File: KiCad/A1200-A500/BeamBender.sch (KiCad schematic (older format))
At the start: 36 parts, among them J1 4-1734742-0, J2 HDMI_A_1.4, J3 STX-3501-3N, J4 Phoenix_Contact, U1 LM1117-3.3, U3 ADV7513BSWZ, X1 Abracon ASE-27.000MHZ-L-R-T

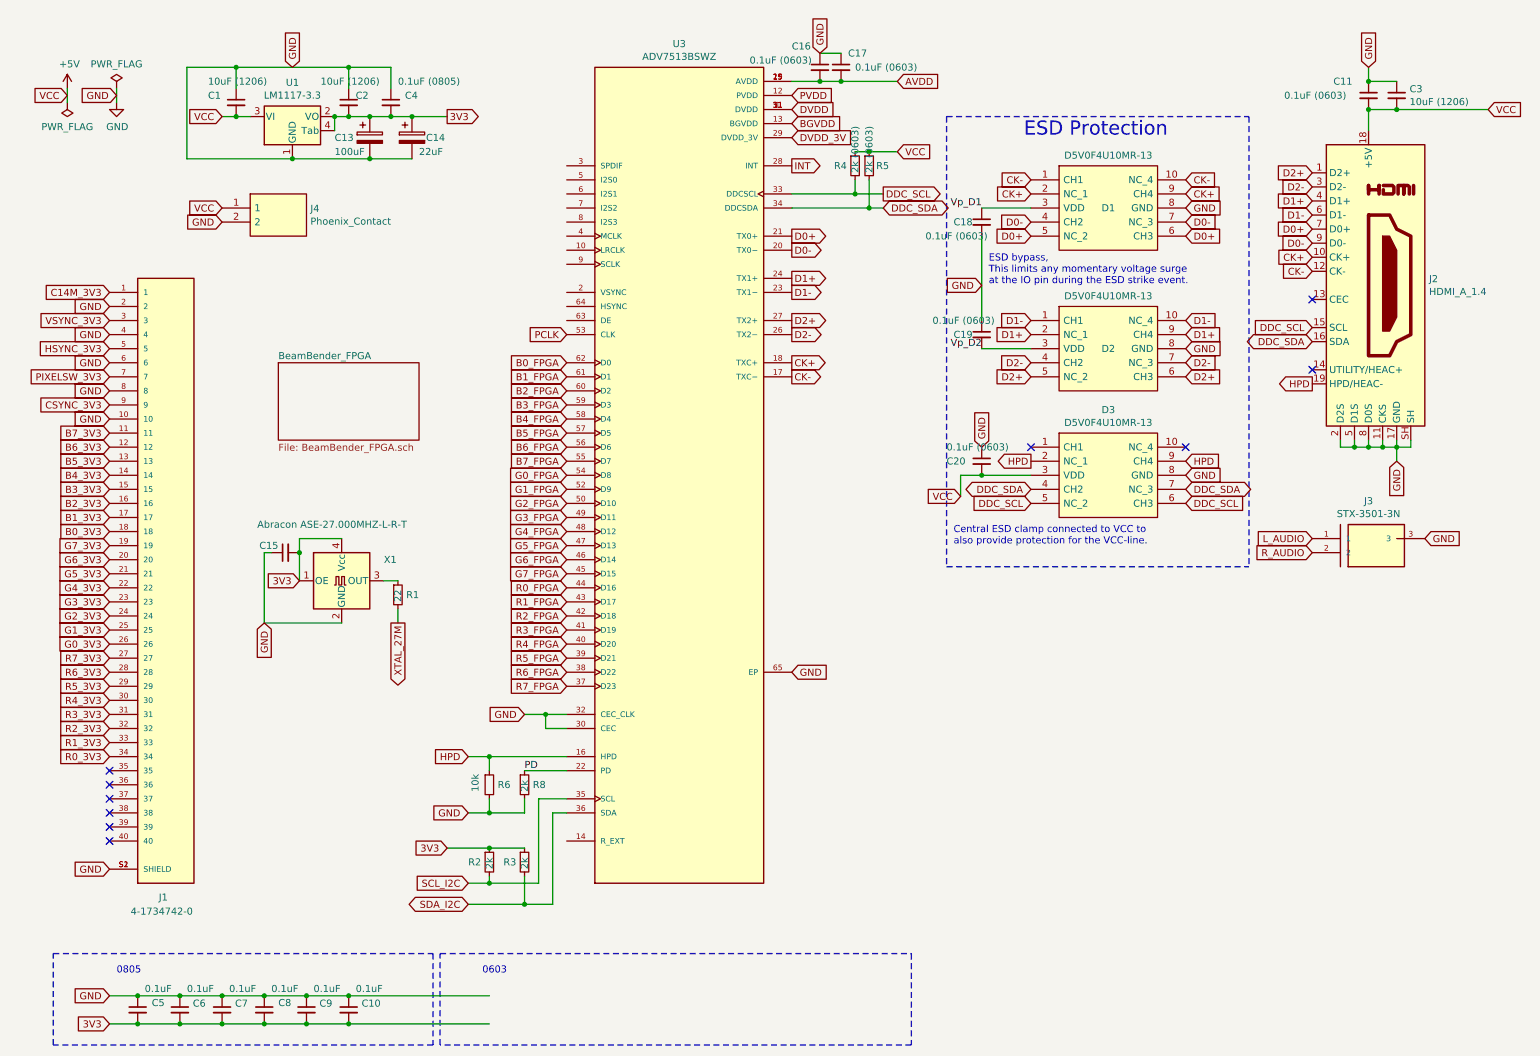
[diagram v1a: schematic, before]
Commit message: more place and route of pull-ups for SDL,SDA,DDC_SDL and DDC_SDA around ADV7513 chip
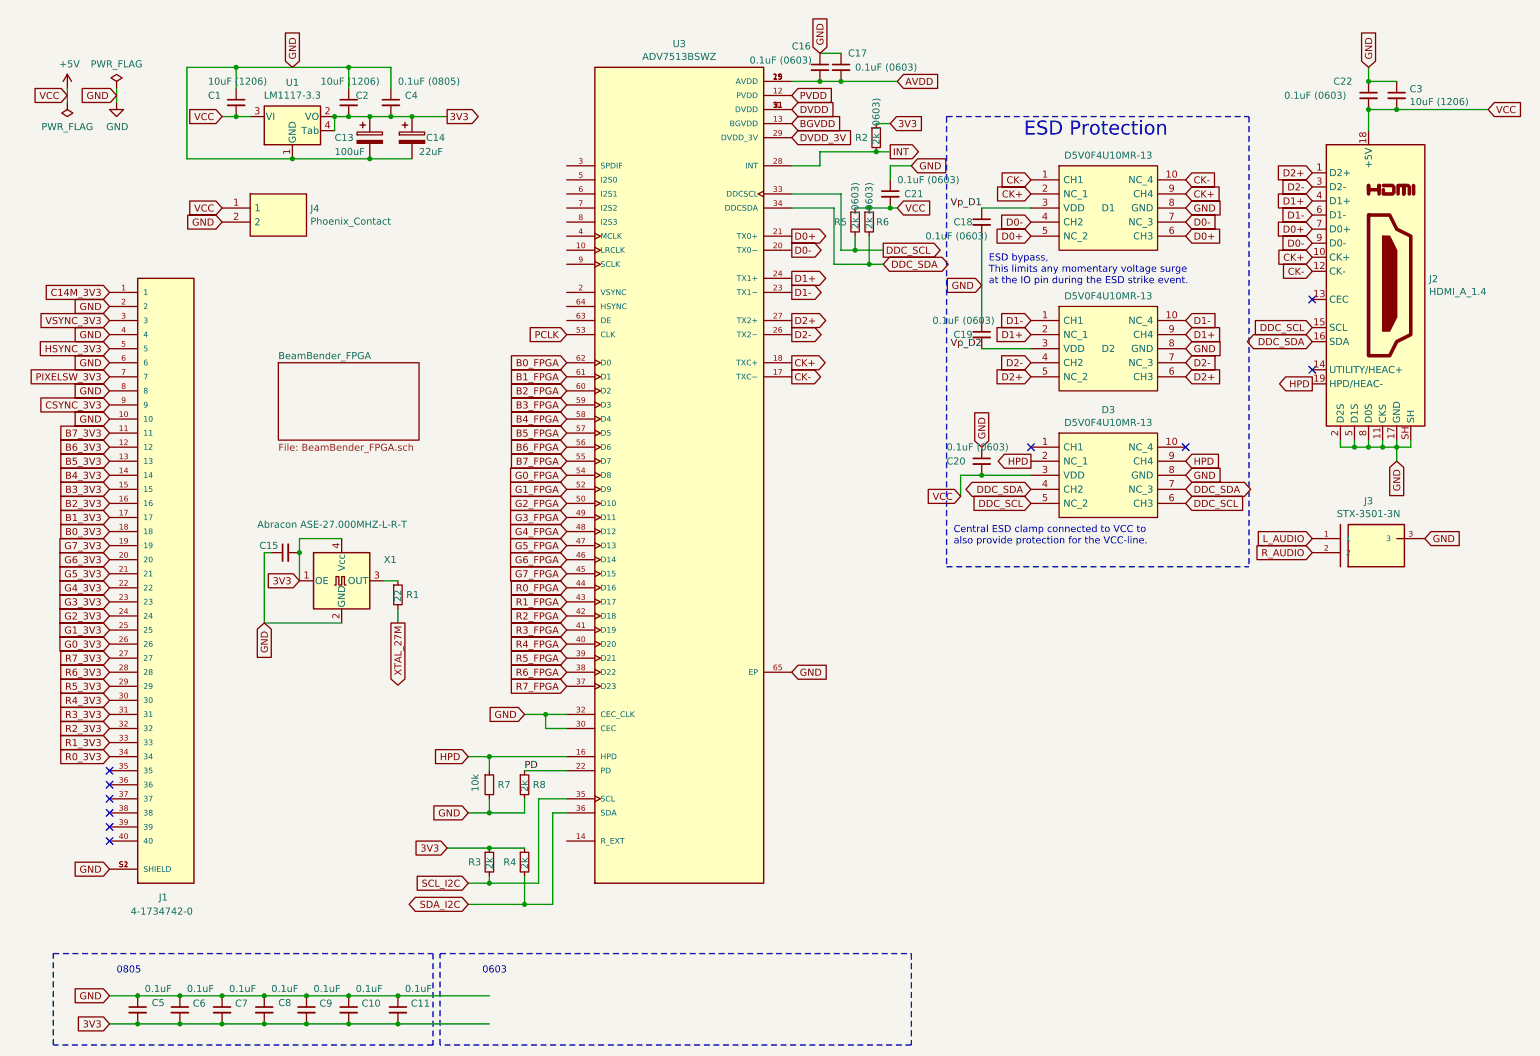
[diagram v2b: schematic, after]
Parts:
- added C11: 0.1uF, Capacitor_SMD:C_0805_2012Metric_Pad1.18x1.45mm_HandSolder, symbol Device:C_Small
- added C21: 0.1uF (0603), Capacitor_SMD:C_0603_1608Metric_Pad1.08x0.95mm_HandSolder, symbol Device:C_Small
- added R2: 2k (0603), Resistor_SMD:R_0603_1608Metric_Pad0.98x0.95mm_HandSolder, symbol Device:R_Small
- renumbered C11 to C22, R2 to R3, R3 to R4, R4 to R5, R5 to R6, R6 to R7
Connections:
- net +5V: now also C21.2
- net 3V3: now also C11.2, R2.1
- net GND: now also C11.1, C21.1
- net INT: now also R2.2
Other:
- moved on the sheet: R5, R6
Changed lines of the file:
@@
 Wire Wire Line
 	10300 3500 10300 3600
-Text GLabel 6650 1700 2    50   Output ~ 0
+Text GLabel 6650 2100 2    50   Output ~ 0
 DDC_SCL
-Text GLabel 6650 1800 2    50   BiDi ~ 0
+Text GLabel 6650 2200 2    50   BiDi ~ 0
 DDC_SDA
 Text GLabel 9700 2750 0    50   BiDi ~ 0
@@
 GND
 $Comp
-L Device:R_Small R4
+L Device:R_Small R5
 U 1 1 6532D8B1
-P 6450 1500
-F 0 "R4" H 6300 1500 50  0000 L CNN
-F 1 "2k  (0603)" V 6450 1450 50  0000 L CNN
-F 2 "Resistor_SMD:R_0603_1608Metric_Pad0.98x0.95mm_HandSolder" H 6450 1500 50  0001 C CNN
-F 3 "~" H 6450 1500 50  0001 C CNN
-	1    6450 1500
-	1    0    0    -1
-$EndComp
-Text GLabel 6750 1400 2    50   Input ~ 0
+P 6450 1900
+F 0 "R5" H 6300 1900 50  0000 L CNN
+F 1 "2k  (0603)" V 6450 1850 50  0000 L CNN
+F 2 "Resistor_SMD:R_0603_1608Metric_Pad0.98x0.95mm_HandSolder" H 6450 1900 50  0001 C CNN
+F 3 "~" H 6450 1900 50  0001 C CNN
+	1    6450 1900
+	1    0    0    -1
+$EndComp
+Text GLabel 6750 1800 2    50   Input ~ 0
 VCC
 Wire Wire Line
-	6450 1600 6450 1700
-Connection ~ 6450 1700
-Wire Wire Line
-	6450 1700 6650 1700
-Wire Wire Line
-	6550 1600 6550 1800
-Connection ~ 6550 1800
-Wire Wire Line
-	6550 1800 6650 1800
+	6450 2000 6450 2100
+Wire Wire Line
+	6450 2100 6650 2100
+Wire Wire Line
+	6550 2000 6550 2200
+Wire Wire Line
+	6550 2200 6650 2200
 Text GLabel 9700 2650 0    50   Input ~ 0
 DDC_SCL
-Wire Wire Line
-	6000 1700 6450 1700
-Wire Wire Line
-	6000 1800 6550 1800
 Text GLabel 4400 2900 0    50   Input ~ 0
 B0_FPGA
@@
 Vp_D1
 $Comp
-L Device:C_Small C11
+L Device:C_Small C22
 U 1 1 654A833A
 P 10100 1000
-F 0 "C11" H 9850 1100 50  0000 L CNN
+F 0 "C22" H 9850 1100 50  0000 L CNN
 F 1 "0.1uF (0603)" H 9500 1000 50  0000 L CNN
 F 2 "Capacitor_SMD:C_0603_1608Metric_Pad1.08x0.95mm_HandSolder" H 10100 1000 50  0001 C CNN
@@
 Connection ~ 3300 1150
 $Comp
-L Device:R_Small R5
+L Device:R_Small R6
 U 1 1 6532BC2D
-P 6550 1500
-F 0 "R5" H 6600 1500 50  0000 L CNN
-F 1 "2k  (0603)" V 6550 1450 50  0000 L CNN
-F 2 "Resistor_SMD:R_0603_1608Metric_Pad0.98x0.95mm_HandSolder" H 6550 1500 50  0001 C CNN
-F 3 "~" H 6550 1500 50  0001 C CNN
-	1    6550 1500
+P 6550 1900
+F 0 "R6" H 6600 1900 50  0000 L CNN
+F 1 "2k  (0603)" V 6550 1850 50  0000 L CNN
+F 2 "Resistor_SMD:R_0603_1608Metric_Pad0.98x0.95mm_HandSolder" H 6550 1900 50  0001 C CNN
+F 3 "~" H 6550 1900 50  0001 C CNN
+	1    6550 1900
 	1    0    0    -1
 $EndComp
@@
 	10300 1100 10950 1100
 Wire Wire Line
-	6450 1400 6550 1400
-Connection ~ 6550 1400
-Wire Wire Line
-	6550 1400 6750 1400
+	6450 1800 6550 1800
+Connection ~ 6550 1800
+Wire Wire Line
+	6550 1800 6700 1800
 Text Notes 1200 7250 0    50   ~ 0
 0805
@@
 GND
 $Comp
-L Device:R_Small R6
+L Device:R_Small R7
 U 1 1 652DC9C5
 P 3850 5900
-F 0 "R6" H 3909 5900 50  0000 L CNN
+F 0 "R7" H 3909 5900 50  0000 L CNN
 F 1 "10k" V 3750 5850 50  0000 L CNN
 F 2 "Resistor_SMD:R_0603_1608Metric_Pad0.98x0.95mm_HandSolder" H 3850 5900 50  0001 C CNN
@@
 	4300 6100 4400 6100
 $Comp
-L Device:R_Small R2
+L Device:R_Small R3
 U 1 1 655C6F45
 P 3850 6450
-F 0 "R2" H 3700 6450 50  0000 L CNN
+F 0 "R3" H 3700 6450 50  0000 L CNN
 F 1 "2k" V 3850 6400 50  0000 L CNN
 F 2 "Resistor_SMD:R_0603_1608Metric_Pad0.98x0.95mm_HandSolder" H 3850 6450 50  0001 C CNN
@@
 	3850 6600 4200 6600
 $Comp
-L Device:R_Small R3
+L Device:R_Small R4
 U 1 1 655D3232
 P 4100 6450
-F 0 "R3" H 3950 6450 50  0000 L CNN
+F 0 "R4" H 3950 6450 50  0000 L CNN
 F 1 "2k" V 4100 6400 50  0000 L CNN
 F 2 "Resistor_SMD:R_0603_1608Metric_Pad0.98x0.95mm_HandSolder" H 4100 6450 50  0001 C CNN
@@
 Wire Wire Line
 	2550 7600 2850 7600
-Text GLabel 6000 1500 2    50   Output ~ 0
+Text GLabel 6700 1400 2    50   Output ~ 0
 INT
 Text GLabel 6000 1000 2    50   Input ~ 0
@@
 Connection ~ 2850 7400
 Wire Wire Line
-	2850 7400 3850 7400
+	2850 7400 3200 7400
 Connection ~ 2850 7600
 Wire Wire Line
-	2850 7600 3850 7600
+	2850 7600 3200 7600
 Text GLabel 4400 2700 0    50   Input ~ 0
 PCLK
+$Comp
+L Device:R_Small R2
+U 1 1 656847D2
+P 6600 1300
+F 0 "R2" H 6450 1300 50  0000 L CNN
+F 1 "2k  (0603)" V 6600 1250 50  0000 L CNN
+F 2 "Resistor_SMD:R_0603_1608Metric_Pad0.98x0.95mm_HandSolder" H 6600 1300 50  0001 C CNN
+F 3 "~" H 6600 1300 50  0001 C CNN
+	1    6600 1300
+	1    0    0    -1
+$EndComp
+Wire Wire Line
+	6450 2100 6350 2100
+Wire Wire Line
+	6350 2100 6350 1700
+Wire Wire Line
+	6350 1700 6000 1700
+Connection ~ 6450 2100
+Wire Wire Line
+	6000 1800 6300 1800
+Wire Wire Line
+	6300 1800 6300 2200
+Wire Wire Line
+	6300 2200 6550 2200
+Connection ~ 6550 2200
+Text GLabel 6700 1200 2    50   Input ~ 0
+3V3
+Wire Wire Line
+	6600 1200 6700 1200
+$Comp
+L Device:C_Small C11
+U 1 1 656BAD96
+P 3200 7500
+F 0 "C11" H 3292 7546 50  0000 L CNN
+F 1 "0.1uF" H 3250 7650 50  0000 L CNN
+F 2 "Capacitor_SMD:C_0805_2012Metric_Pad1.18x1.45mm_HandSolder" H 3200 7500 50  0001 C CNN
+F 3 "~" H 3200 7500 50  0001 C CNN
+	1    3200 7500
+	1    0    0    -1
+$EndComp
+Connection ~ 3200 7400
+Wire Wire Line
+	3200 7400 3850 7400
+Connection ~ 3200 7600
+Wire Wire Line
+	3200 7600 3850 7600
+$Comp
+L Device:C_Small C21
+U 1 1 656E4A42
+P 6700 1700
+F 0 "C21" H 6800 1700 50  0000 L CNN
+F 1 "0.1uF (0603)" H 6750 1800 50  0000 L CNN
+F 2 "Capacitor_SMD:C_0603_1608Metric_Pad1.08x0.95mm_HandSolder" H 6700 1700 50  0001 C CNN
+F 3 "~" H 6700 1700 50  0001 C CNN
+	1    6700 1700
+	1    0    0    -1
+$EndComp
+Connection ~ 6700 1800
+Wire Wire Line
+	6700 1800 6750 1800
+Text GLabel 6850 1500 2    50   Input ~ 0
+GND
+Wire Wire Line
+	6000 1500 6200 1500
+Wire Wire Line
+	6200 1500 6200 1400
+Wire Wire Line
+	6200 1400 6600 1400
+Wire Wire Line
+	6700 1600 6700 1500
+Wire Wire Line
+	6700 1500 6850 1500
+Wire Wire Line
+	6600 1400 6700 1400
+Connection ~ 6600 1400
 $EndSCHEMATC

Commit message: more routing done
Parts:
- added C12: 10uF (1206), Capacitor_SMD:C_1206_3216Metric_Pad1.33x1.80mm_HandSolder, symbol Device:C_Small
- added C23: 0.1uF (0603), Capacitor_SMD:C_0603_1608Metric_Pad1.08x0.95mm_HandSolder, symbol Device:C_Small
- added C?: 0.1uF, Capacitor_SMD:C_0603_1608Metric_Pad1.08x0.95mm_HandSolder, symbol Device:C_Small
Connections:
- net 3V3: now also C?.2
- net DVDD: now also C12.1, C23.1
- net GND: now also C12.2, C23.2, C?.1
- net VSYNC_FPGA: now reaches U3.2 (VSYNC)
- net DE: now reaches U3.63 (DE)
- net HSYNC_FPGA: now reaches U3.64 (HSYNC)
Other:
- moved on the sheet: C11
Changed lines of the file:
@@
 	10200 3500 10300 3500
 NoConn ~ 9700 2950
-Text GLabel 6750 900  2    50   Input ~ 0
-AVDD
 Wire Wire Line
 	6000 900  6200 900
@@
 Wire Wire Line
 	6200 900  6350 900
-$Comp
-L Device:C_Small C17
-U 1 1 653F698E
-P 6350 800
-F 0 "C17" H 6400 900 50  0000 L CNN
-F 1 "0.1uF (0603)" H 6450 800 50  0000 L CNN
-F 2 "Capacitor_SMD:C_0603_1608Metric_Pad1.08x0.95mm_HandSolder" H 6350 800 50  0001 C CNN
-F 3 "~" H 6350 800 50  0001 C CNN
-	1    6350 800
-	1    0    0    -1
-$EndComp
-Connection ~ 6350 900
-Wire Wire Line
-	6350 900  6750 900
 Wire Wire Line
 	6200 700  6350 700
@@
 Text GLabel 6000 1000 2    50   Input ~ 0
 PVDD
-Text GLabel 6000 1100 2    50   Input ~ 0
-DVDD
 Text GLabel 6000 1300 2    50   Input ~ 0
 DVDD_3V
@@
 Connection ~ 2850 7400
 Wire Wire Line
-	2850 7400 3200 7400
+	2850 7400 3150 7400
 Connection ~ 2850 7600
 Wire Wire Line
-	2850 7600 3200 7600
+	2850 7600 3150 7600
 Text GLabel 4400 2700 0    50   Input ~ 0
 PCLK
@@
 L Device:C_Small C11
 U 1 1 656BAD96
-P 3200 7500
-F 0 "C11" H 3292 7546 50  0000 L CNN
-F 1 "0.1uF" H 3250 7650 50  0000 L CNN
-F 2 "Capacitor_SMD:C_0805_2012Metric_Pad1.18x1.45mm_HandSolder" H 3200 7500 50  0001 C CNN
-F 3 "~" H 3200 7500 50  0001 C CNN
-	1    3200 7500
-	1    0    0    -1
-$EndComp
-Connection ~ 3200 7400
-Wire Wire Line
-	3200 7400 3850 7400
-Connection ~ 3200 7600
-Wire Wire Line
-	3200 7600 3850 7600
+P 3150 7500
+F 0 "C11" H 3242 7546 50  0000 L CNN
+F 1 "0.1uF" H 3200 7650 50  0000 L CNN
+F 2 "Capacitor_SMD:C_0805_2012Metric_Pad1.18x1.45mm_HandSolder" H 3150 7500 50  0001 C CNN
+F 3 "~" H 3150 7500 50  0001 C CNN
+	1    3150 7500
+	1    0    0    -1
+$EndComp
 $Comp
 L Device:C_Small C21
@@
 	6600 1400 6700 1400
 Connection ~ 6600 1400
+Connection ~ 3150 7400
+Connection ~ 3150 7600
+Wire Wire Line
+	3150 7400 3850 7400
+Wire Wire Line
+	3150 7600 3850 7600
+$Comp
+L Device:C_Small C17
+U 1 1 653F698E
+P 6350 800
+F 0 "C17" H 6400 900 50  0000 L CNN
+F 1 "0.1uF (0603)" H 6450 800 50  0000 L CNN
+F 2 "Capacitor_SMD:C_0603_1608Metric_Pad1.08x0.95mm_HandSolder" H 6350 800 50  0001 C CNN
+F 3 "~" H 6350 800 50  0001 C CNN
+	1    6350 800
+	1    0    0    -1
+$EndComp
+Text GLabel 6000 1100 2    50   Input ~ 0
+DVDD
+Connection ~ 6350 900
+Wire Wire Line
+	6350 900  6750 900
+Text GLabel 6750 900  2    50   Input ~ 0
+AVDD
+$Comp
+L Device:C_Small C12
+U 1 1 657943FC
+P 7900 5050
+F 0 "C12" H 7700 5150 50  0000 L CNN
+F 1 "10uF (1206)" H 7700 4950 50  0000 L CNN
+F 2 "Capacitor_SMD:C_1206_3216Metric_Pad1.33x1.80mm_HandSolder" H 7900 5050 50  0001 C CNN
+F 3 "~" H 7900 5050 50  0001 C CNN
+	1    7900 5050
+	1    0    0    -1
+$EndComp
+Text GLabel 8050 4900 1    50   Input ~ 0
+DVDD
+$Comp
+L Device:C_Small C23
+U 1 1 65796712
+P 8300 5050
+F 0 "C23" H 8150 5150 50  0000 L CNN
+F 1 "0.1uF (0603)" H 8150 5250 50  0000 L CNN
+F 2 "Capacitor_SMD:C_0603_1608Metric_Pad1.08x0.95mm_HandSolder" H 8300 5050 50  0001 C CNN
+F 3 "~" H 8300 5050 50  0001 C CNN
+	1    8300 5050
+	1    0    0    -1
+$EndComp
+Wire Wire Line
+	7900 4900 8300 4900
+Text GLabel 7900 5200 3    50   Input ~ 0
+GND
+Connection ~ 8300 4900
+Wire Wire Line
+	8300 4900 8550 4900
+Wire Wire Line
+	7900 5200 8300 5200
+Text GLabel 4400 2600 0    50   Input ~ 0
+DE
+Text GLabel 4400 2400 0    50   Input ~ 0
+VSYNC_FPGA
+Text GLabel 4400 2500 0    50   Input ~ 0
+HSYNC_FPGA
+Wire Wire Line
+	8300 4950 8300 4900
+Wire Wire Line
+	8300 5150 8300 5200
+Wire Wire Line
+	7900 4950 7900 4900
+Wire Wire Line
+	7900 5150 7900 5200
+$Comp
+L Device:C_Small C?
+U 1 1 6584F5FE
+P 3850 7500
+F 0 "C?" H 3700 7550 50  0000 L CNN
+F 1 "0.1uF" H 3700 7650 50  0000 L CNN
+F 2 "Capacitor_SMD:C_0603_1608Metric_Pad1.08x0.95mm_HandSolder" H 3850 7500 50  0001 C CNN
+F 3 "~" H 3850 7500 50  0001 C CNN
+	1    3850 7500
+	1    0    0    -1
+$EndComp
 $EndSCHEMATC
